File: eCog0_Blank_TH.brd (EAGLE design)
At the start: 47.5 x 28 mm, 3 parts

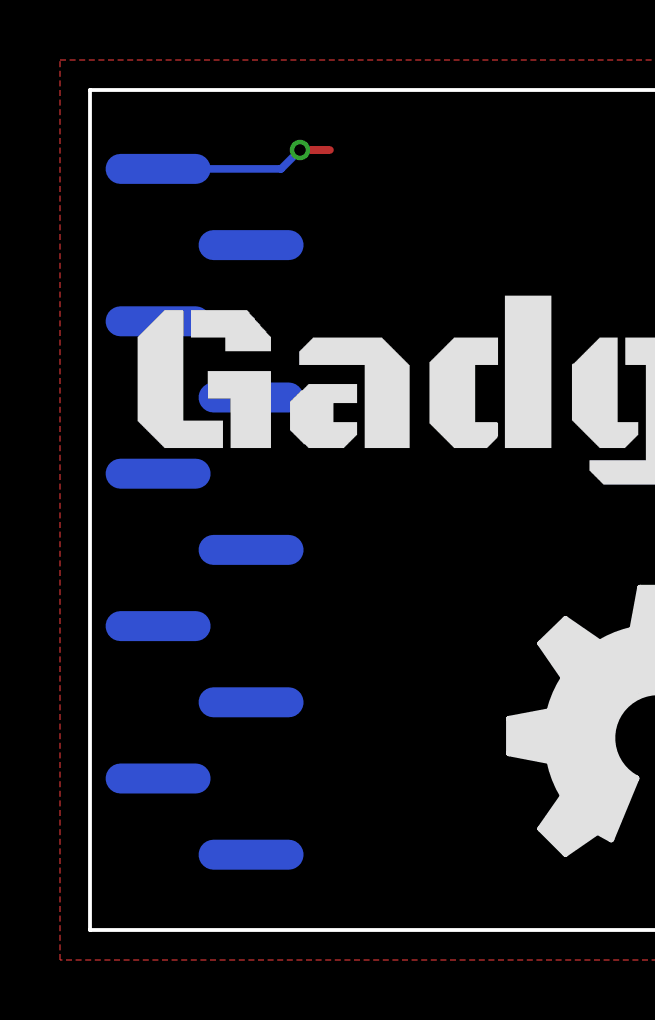
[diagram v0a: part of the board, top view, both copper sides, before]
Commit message: Added new eCogs
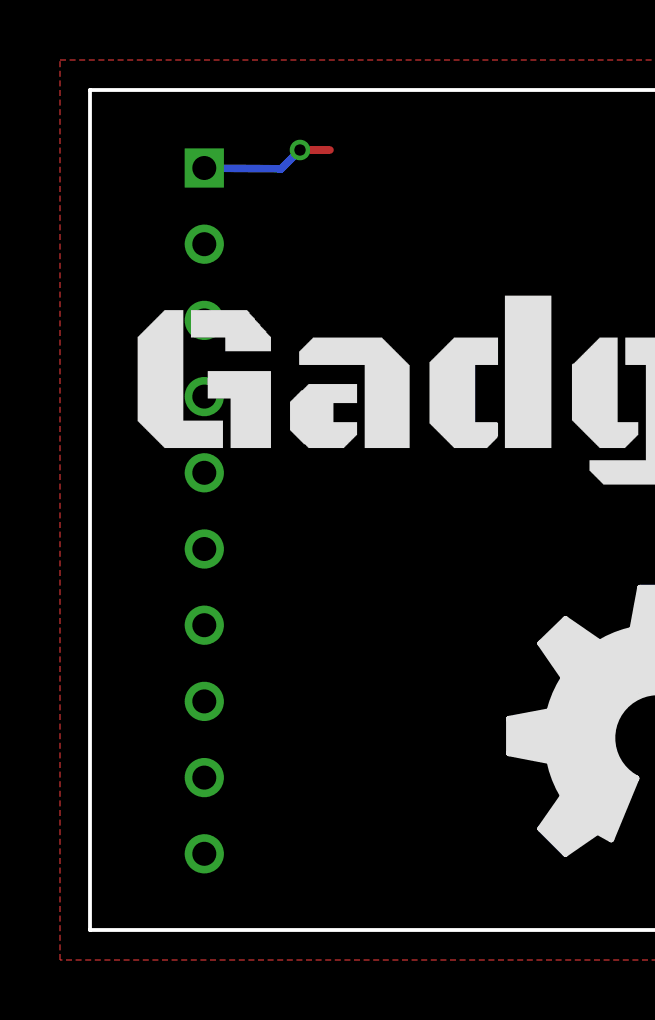
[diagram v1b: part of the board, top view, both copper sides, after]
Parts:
- ECOG: value ECOG_GENERAL_ROWECOG_GENERAL_SMD -> ECOG_GENERAL_ROWECOG_GENERAL_TH; device eCogs:ECOG_GENERAL_SMD -> eCogs:ECOG_GENERAL_TH
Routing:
- net GND: track 5.99 -> 4.45 mm
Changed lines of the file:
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@@
 </autorouter>
 <elements>
-<element name="ECOG" library="eCogs" package="ECOG_GENERAL_SMD" value="ECOG_GENERAL_ROWECOG_GENERAL_SMD" x="0" y="0" smashed="yes">
-<attribute name="DIGIKEY" value="S1013EC-10-ND" x="0" y="0" size="1.778" layer="27" display="off"/>
-</element>
+<element name="ECOG" library="eCogs" package="ECOG_GENERAL_TH" value="ECOG_GENERAL_ROWECOG_GENERAL_TH" x="0" y="0" smashed="yes"/>
 <element name="U$2" library="GadgetFactory" package="GADGETBOX_TEXT" value="" x="22.86" y="17.78"/>
 <element name="U$1" library="ohw-logo" package="OSHW_FILLX350_NOTEXT" value="" x="13.97" y="2.54"/>
@@
 <vertex x="-1" y="-1"/>
 </polygon>
-<wire x1="2.2706" y1="25.37" x2="6.37" y2="25.37" width="0.254" layer="16"/>
+<wire x1="3.81" y1="25.4" x2="6.37" y2="25.37" width="0.254" layer="16"/>
 <wire x1="6.37" y1="25.37" x2="7" y2="26" width="0.254" layer="16"/>
 <via x="7" y="26" extent="1-16" drill="0.381"/>
